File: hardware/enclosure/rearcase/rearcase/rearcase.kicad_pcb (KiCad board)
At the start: 2 copper layers, 42.5 x 23 mm, 1 part

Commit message: serial enclosure
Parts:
- removed the REF** at (154.0, 98.0)
- added REF**: rearpanell, ps2pcb:rearpanell, F.Cu at (153.8, 96.5)
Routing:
- net GND: vias 5 -> 0
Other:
- board size 42.5 x 23 mm -> 63.5 x 30 mm

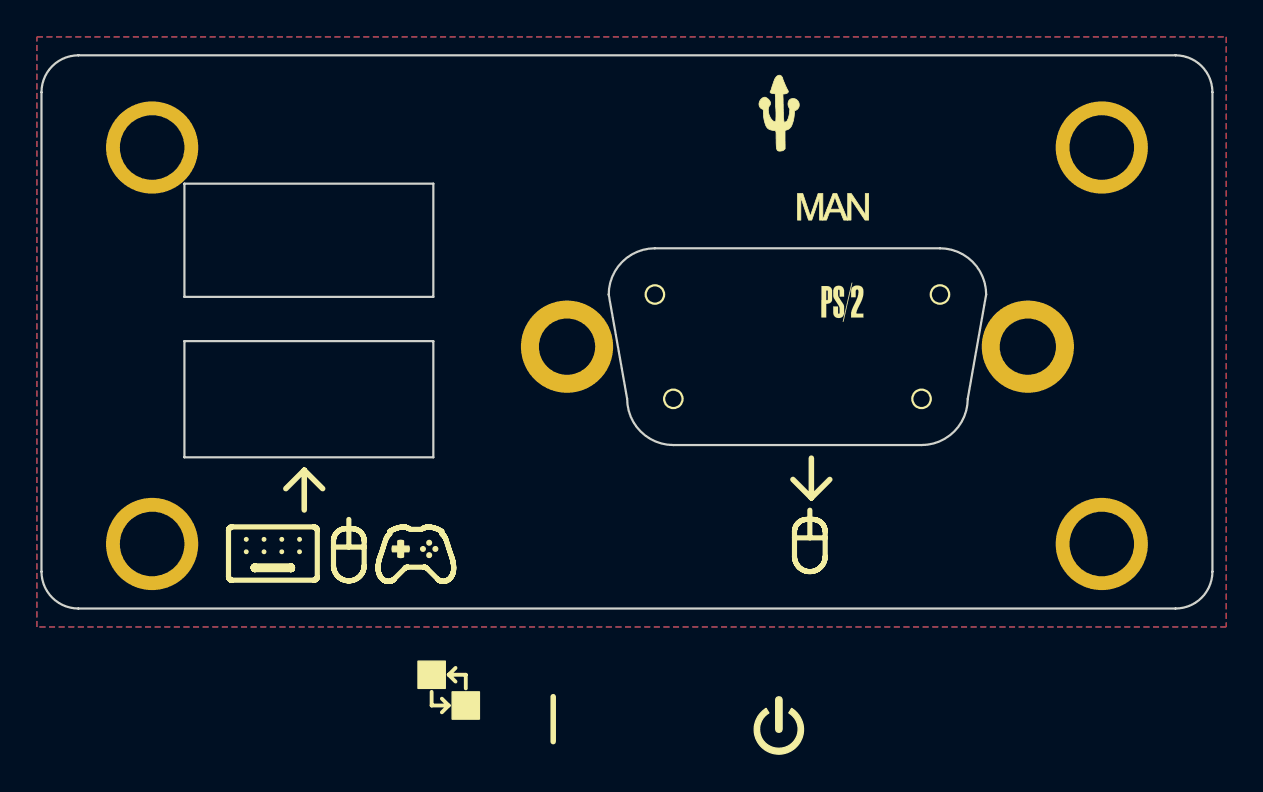
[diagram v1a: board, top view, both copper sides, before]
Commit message: Serial version board/enclosure rework
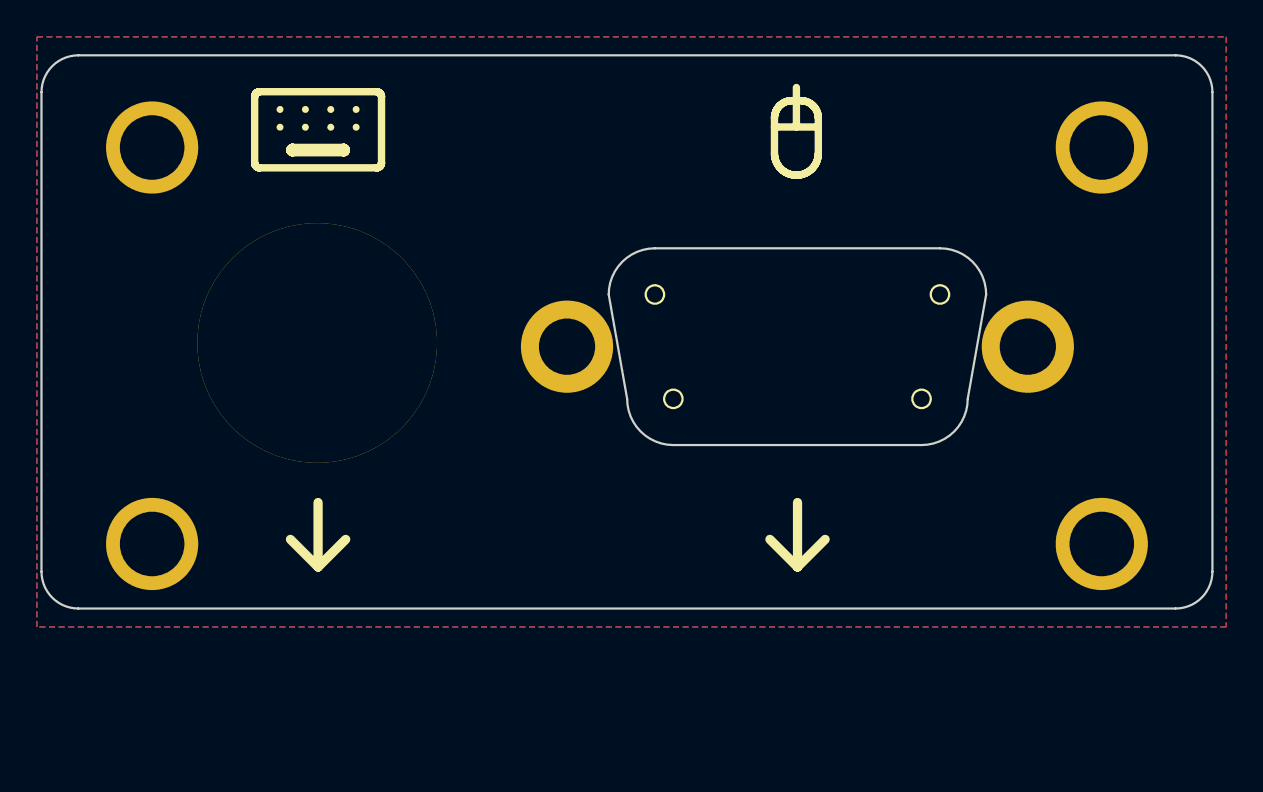
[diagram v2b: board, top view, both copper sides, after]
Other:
- outline, holes or cut-outs redrawn

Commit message: Finished serial enclosure
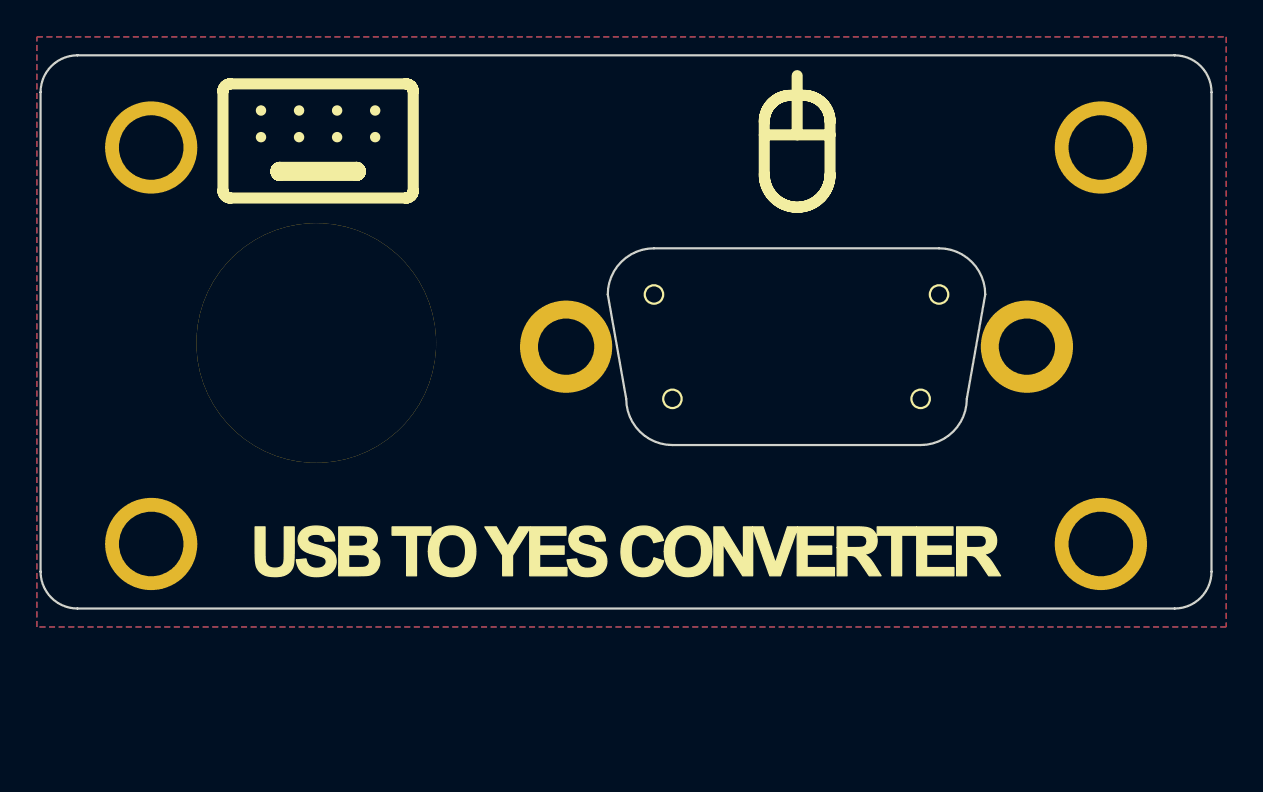
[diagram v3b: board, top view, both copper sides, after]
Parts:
- moved REF** 0.05 mm to (153.7, 96.5)
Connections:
- REF** pad 2: (no net) -> GND
